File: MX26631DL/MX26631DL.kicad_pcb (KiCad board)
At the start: 4 copper layers, 21 x 22.6 mm, 13 parts, among them U2 MX26631DL, U4 TPESD0402G15V

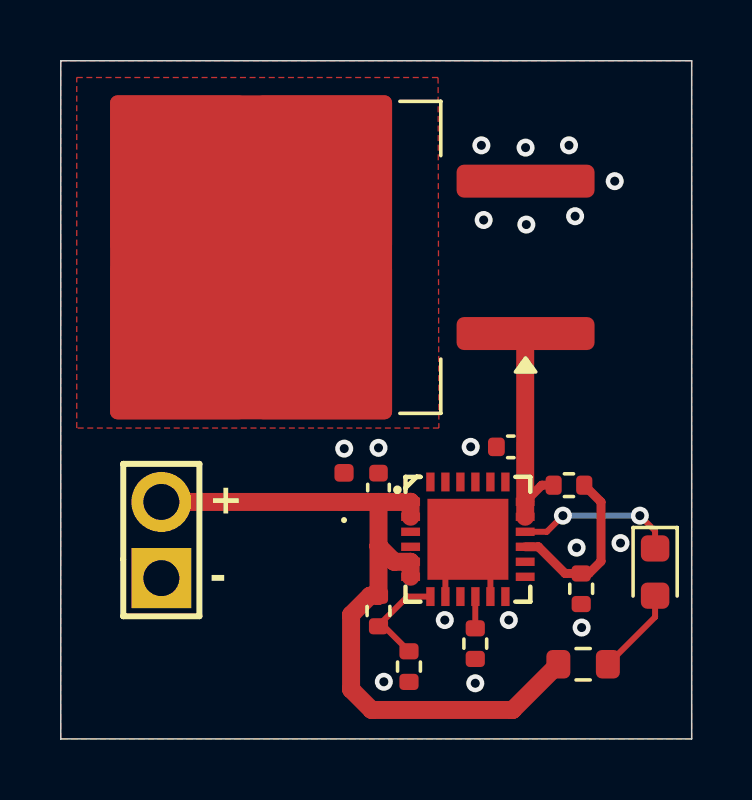
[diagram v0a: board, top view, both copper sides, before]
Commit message: Removed Ground pour for easier sodering
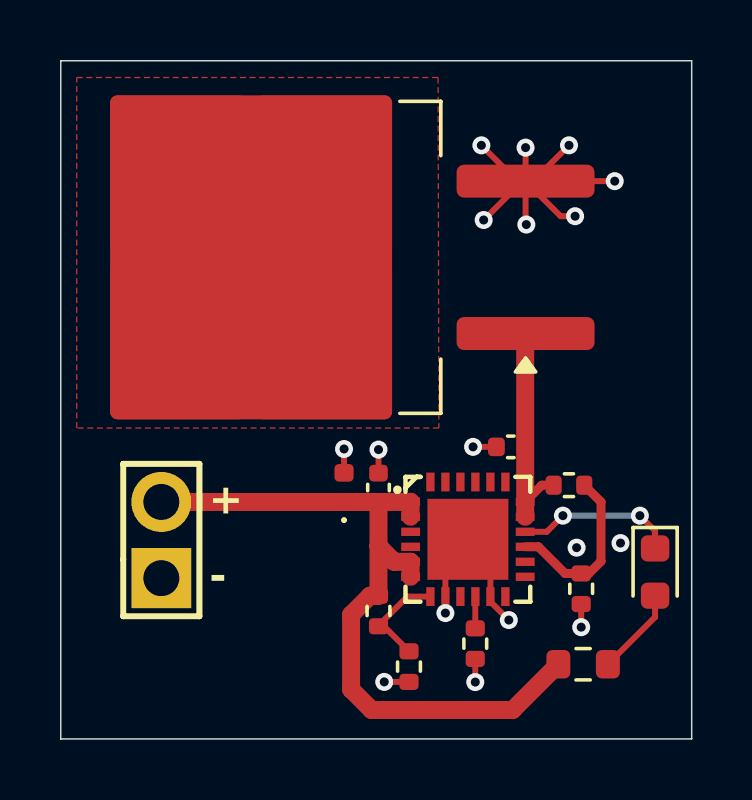
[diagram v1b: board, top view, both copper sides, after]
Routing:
- net GND: track 4.44 -> 24.3 mm
- removed copper zone on F.Cu, net GND
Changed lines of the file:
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@@
+	)
+	(segment
+		(start 107.2588 96.44)
+		(end 107.2588 95.89)
+		(width 0.2)
+		(layer "F.Cu")
+		(net 2)
+	)
+	(segment
+		(start 111.7854 96.139)
+		(end 111.7854 96.91)
+		(width 0.2)
+		(layer "F.Cu")
+		(net 2)
+	)
+	(segment
+		(start 108.2548 97.9678)
+		(end 108.2548 98.74)
+		(width 0.2)
+		(layer "F.Cu")
+		(net 2)
+	)
+	(segment
+		(start 108.9588 90.899357)
+		(end 108.18 90.899357)
+		(width 0.2)
+		(layer "F.Cu")
+		(net 2)
+	)
+	(segment
+		(start 103.88 91.765361)
+		(end 103.880039 91.7654)
+		(width 0.2)
+		(layer "F.Cu")
+		(net 2)
+	)
+	(segment
+		(start 103.88 90.97)
+		(end 103.88 91.765361)
+		(width 0.2)
+		(layer "F.Cu")
+		(net 2)
+	)
+	(segment
+		(start 110.1852 82.042)
+		(end 111.379 80.8482)
+		(width 0.2)
+		(layer "F.Cu")
+		(net 2)
+	)
+	(segment
+		(start 109.8296 82.042)
+		(end 108.5342 83.3374)
+		(width 0.2)
+		(layer "F.Cu")
+		(net 2)
 	)
 	(segment
@@
 	)
 	(segment
+		(start 108.7588 96.0588)
+		(end 109.3724 96.6724)
+		(width 0.2)
+		(layer "F.Cu")
+		(net 2)
+	)
+	(segment
 		(start 107.2588 94.73)
 		(end 107.2588 95.89)
@@
 	)
 	(segment
+		(start 108.7588 95.89)
+		(end 108.7588 96.0588)
+		(width 0.2)
+		(layer "F.Cu")
+		(net 2)
+	)
+	(segment
+		(start 109.9312 82.042)
+		(end 112.903 82.042)
+		(width 0.2)
+		(layer "F.Cu")
+		(net 2)
+	)
+	(segment
+		(start 109.9312 82.042)
+		(end 109.9312 80.9244)
+		(width 0.2)
+		(layer "F.Cu")
+		(net 2)
+	)
+	(segment
+		(start 109.9312 82.042)
+		(end 111.0996 83.2104)
+		(width 0.2)
+		(layer "F.Cu")
+		(net 2)
+	)
+	(segment
 		(start 108.0088 93.98)
 		(end 108.7588 94.73)
@@
 		(net 2)
 	)
+	(segment
+		(start 109.9312 83.4644)
+		(end 109.9566 83.4898)
+		(width 0.2)
+		(layer "F.Cu")
+		(net 2)
+	)
+	(segment
+		(start 109.9312 82.042)
+		(end 109.6518 82.042)
+		(width 0.2)
+		(layer "F.Cu")
+		(net 2)
+	)
+	(segment
+		(start 109.9312 82.042)
+		(end 109.9312 83.4644)
+		(width 0.2)
+		(layer "F.Cu")
+		(net 2)
+	)
+	(segment
+		(start 106.045 98.7338)
+		(end 105.22 98.7338)
+		(width 0.2)
+		(layer "F.Cu")
+		(net 2)
+	)
+	(segment
+		(start 109.9312 82.042)
+		(end 110.1852 82.042)
+		(width 0.2)
+		(layer "F.Cu")
+		(net 2)
+	)
+	(segment
+		(start 111.0996 83.2104)
+		(end 111.5822 83.2104)
+		(width 0.2)
+		(layer "F.Cu")
+		(net 2)
+	)
+	(segment
+		(start 109.9312 82.042)
+		(end 109.8296 82.042)
+		(width 0.2)
+		(layer "F.Cu")
+		(net 2)
+	)
+	(segment
+		(start 105.029 90.99)
+		(end 105.029 91.7754)
+		(width 0.2)
+		(layer "F.Cu")
+		(net 2)
+	)
+	(segment
+		(start 109.6518 82.042)
+		(end 108.458 80.8482)
+		(width 0.2)
+		(layer "F.Cu")
+		(net 2)
+	)
 	(via
 		(at 109.9312 80.9244)
@@
 	)
 	(via
-		(at 107.2388 96.6724)
+		(at 107.2588 96.44)
 		(size 0.6)
 		(drill 0.3)
@@
 	)
 	(via
-		(at 105.2068 98.7298)
+		(at 105.22 98.7338)
 		(size 0.6)
 		(drill 0.3)
@@
 	)
 	(via
-		(at 103.886 90.9574)
-		(size 0.6)
-		(drill 0.3)
-		(layers "F.Cu" "B.Cu")
-		(free yes)
-		(net 2)
-	)
-	(via
-		(at 108.2548 98.779685)
+		(at 103.88 90.97)
+		(size 0.6)
+		(drill 0.3)
+		(layers "F.Cu" "B.Cu")
+		(free yes)
+		(net 2)
+	)
+	(via
+		(at 108.2548 98.74)
 		(size 0.6)
 		(drill 0.3)
@@
 	)
 	(via
-		(at 105.029 90.932)
-		(size 0.6)
-		(drill 0.3)
-		(layers "F.Cu" "B.Cu")
-		(free yes)
-		(net 2)
-	)
-	(via
-		(at 108.1024 90.899357)
-		(size 0.6)
-		(drill 0.3)
-		(layers "F.Cu" "B.Cu")
-		(net 2)
-	)
-	(via
-		(at 111.799587 96.9224)
+		(at 105.029 90.99)
+		(size 0.6)
+		(drill 0.3)
+		(layers "F.Cu" "B.Cu")
+		(free yes)
+		(net 2)
+	)
+	(via
+		(at 108.18 90.899357)
+		(size 0.6)
+		(drill 0.3)
+		(layers "F.Cu" "B.Cu")
+		(net 2)
+	)
+	(via
+		(at 111.7854 96.91)
 		(size 0.6)
 		(drill 0.3)
@@
 	)
 	(zone
-		(net 2)
-		(net_name "GND")
-		(layer "F.Cu")
-		(hatch edge 0.5)
-		(connect_pads yes
-			(clearance 0.1)
-		)
-		(min_thickness 0.1)
-		(filled_areas_thickness no)
-		(fill yes
-			(thermal_gap 0.5)
-			(thermal_bridge_width 0.5)
-		)
-		(polygon
-			(pts
-				(xy 94.4372 78.0288) (xy 115.4684 78.0288) (xy 115.4684 100.6348) (xy 94.4372 100.6348)
-			)
-		)
-	)
-	(zone

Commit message: Revert "Removed Ground pour for easier sodering"
This reverts commit 94e415ae81cb2b8cab0b706f2261028b2c6a871a.
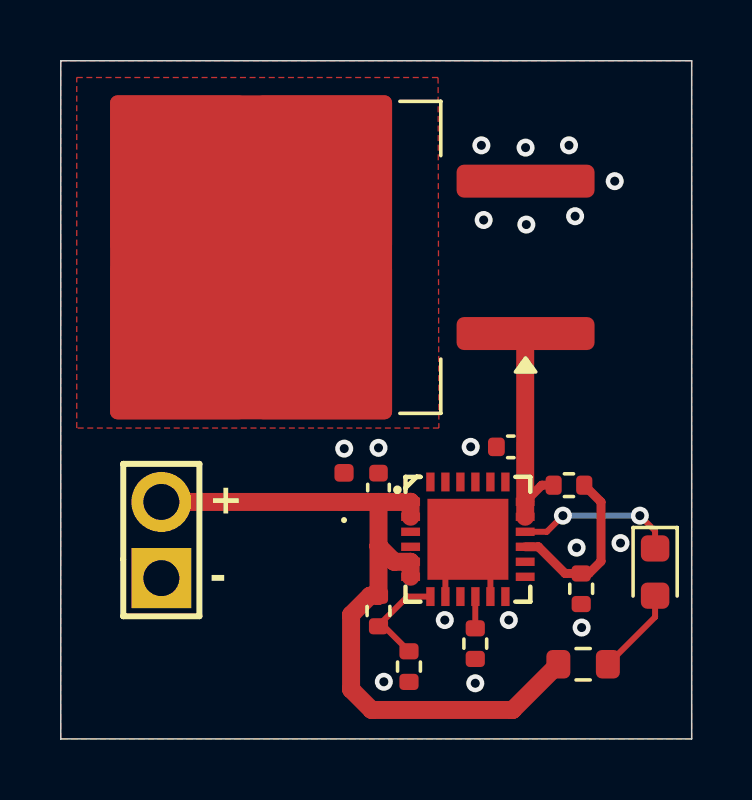
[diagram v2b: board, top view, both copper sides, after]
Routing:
- net GND: track 24.3 -> 4.44 mm
- added copper zone on F.Cu, net GND
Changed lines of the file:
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@@
-	)
-	(segment
-		(start 107.2588 96.44)
-		(end 107.2588 95.89)
-		(width 0.2)
-		(layer "F.Cu")
-		(net 2)
-	)
-	(segment
-		(start 111.7854 96.139)
-		(end 111.7854 96.91)
-		(width 0.2)
-		(layer "F.Cu")
-		(net 2)
-	)
-	(segment
-		(start 108.2548 97.9678)
-		(end 108.2548 98.74)
-		(width 0.2)
-		(layer "F.Cu")
-		(net 2)
-	)
-	(segment
-		(start 108.9588 90.899357)
-		(end 108.18 90.899357)
-		(width 0.2)
-		(layer "F.Cu")
-		(net 2)
-	)
-	(segment
-		(start 103.88 91.765361)
-		(end 103.880039 91.7654)
-		(width 0.2)
-		(layer "F.Cu")
-		(net 2)
-	)
-	(segment
-		(start 103.88 90.97)
-		(end 103.88 91.765361)
-		(width 0.2)
-		(layer "F.Cu")
-		(net 2)
-	)
-	(segment
-		(start 110.1852 82.042)
-		(end 111.379 80.8482)
-		(width 0.2)
-		(layer "F.Cu")
-		(net 2)
-	)
-	(segment
-		(start 109.8296 82.042)
-		(end 108.5342 83.3374)
-		(width 0.2)
-		(layer "F.Cu")
-		(net 2)
 	)
 	(segment
@@
 	)
 	(segment
-		(start 108.7588 96.0588)
-		(end 109.3724 96.6724)
-		(width 0.2)
-		(layer "F.Cu")
-		(net 2)
-	)
-	(segment
 		(start 107.2588 94.73)
 		(end 107.2588 95.89)
@@
 	)
 	(segment
-		(start 108.7588 95.89)
-		(end 108.7588 96.0588)
-		(width 0.2)
-		(layer "F.Cu")
-		(net 2)
-	)
-	(segment
-		(start 109.9312 82.042)
-		(end 112.903 82.042)
-		(width 0.2)
-		(layer "F.Cu")
-		(net 2)
-	)
-	(segment
-		(start 109.9312 82.042)
-		(end 109.9312 80.9244)
-		(width 0.2)
-		(layer "F.Cu")
-		(net 2)
-	)
-	(segment
-		(start 109.9312 82.042)
-		(end 111.0996 83.2104)
-		(width 0.2)
-		(layer "F.Cu")
-		(net 2)
-	)
-	(segment
 		(start 108.0088 93.98)
 		(end 108.7588 94.73)
@@
 		(net 2)
 	)
-	(segment
-		(start 109.9312 83.4644)
-		(end 109.9566 83.4898)
-		(width 0.2)
-		(layer "F.Cu")
-		(net 2)
-	)
-	(segment
-		(start 109.9312 82.042)
-		(end 109.6518 82.042)
-		(width 0.2)
-		(layer "F.Cu")
-		(net 2)
-	)
-	(segment
-		(start 109.9312 82.042)
-		(end 109.9312 83.4644)
-		(width 0.2)
-		(layer "F.Cu")
-		(net 2)
-	)
-	(segment
-		(start 106.045 98.7338)
-		(end 105.22 98.7338)
-		(width 0.2)
-		(layer "F.Cu")
-		(net 2)
-	)
-	(segment
-		(start 109.9312 82.042)
-		(end 110.1852 82.042)
-		(width 0.2)
-		(layer "F.Cu")
-		(net 2)
-	)
-	(segment
-		(start 111.0996 83.2104)
-		(end 111.5822 83.2104)
-		(width 0.2)
-		(layer "F.Cu")
-		(net 2)
-	)
-	(segment
-		(start 109.9312 82.042)
-		(end 109.8296 82.042)
-		(width 0.2)
-		(layer "F.Cu")
-		(net 2)
-	)
-	(segment
-		(start 105.029 90.99)
-		(end 105.029 91.7754)
-		(width 0.2)
-		(layer "F.Cu")
-		(net 2)
-	)
-	(segment
-		(start 109.6518 82.042)
-		(end 108.458 80.8482)
-		(width 0.2)
-		(layer "F.Cu")
-		(net 2)
-	)
 	(via
 		(at 109.9312 80.9244)
@@
 	)
 	(via
-		(at 107.2588 96.44)
+		(at 107.2388 96.6724)
 		(size 0.6)
 		(drill 0.3)
@@
 	)
 	(via
-		(at 105.22 98.7338)
+		(at 105.2068 98.7298)
 		(size 0.6)
 		(drill 0.3)
@@
 	)
 	(via
-		(at 103.88 90.97)
-		(size 0.6)
-		(drill 0.3)
-		(layers "F.Cu" "B.Cu")
-		(free yes)
-		(net 2)
-	)
-	(via
-		(at 108.2548 98.74)
+		(at 103.886 90.9574)
+		(size 0.6)
+		(drill 0.3)
+		(layers "F.Cu" "B.Cu")
+		(free yes)
+		(net 2)
+	)
+	(via
+		(at 108.2548 98.779685)
 		(size 0.6)
 		(drill 0.3)
@@
 	)
 	(via
-		(at 105.029 90.99)
-		(size 0.6)
-		(drill 0.3)
-		(layers "F.Cu" "B.Cu")
-		(free yes)
-		(net 2)
-	)
-	(via
-		(at 108.18 90.899357)
-		(size 0.6)
-		(drill 0.3)
-		(layers "F.Cu" "B.Cu")
-		(net 2)
-	)
-	(via
-		(at 111.7854 96.91)
+		(at 105.029 90.932)
+		(size 0.6)
+		(drill 0.3)
+		(layers "F.Cu" "B.Cu")
+		(free yes)
+		(net 2)
+	)
+	(via
+		(at 108.1024 90.899357)
+		(size 0.6)
+		(drill 0.3)
+		(layers "F.Cu" "B.Cu")
+		(net 2)
+	)
+	(via
+		(at 111.799587 96.9224)
 		(size 0.6)
 		(drill 0.3)
@@
 	)
 	(zone
+		(net 2)
+		(net_name "GND")
+		(layer "F.Cu")
+		(hatch edge 0.5)
+		(connect_pads yes
+			(clearance 0.1)
+		)
+		(min_thickness 0.1)
+		(filled_areas_thickness no)
+		(fill yes
+			(thermal_gap 0.5)
+			(thermal_bridge_width 0.5)
+		)
+		(polygon
+			(pts
+				(xy 94.4372 78.0288) (xy 115.4684 78.0288) (xy 115.4684 100.6348) (xy 94.4372 100.6348)
+			)
+		)
+	)
+	(zone
